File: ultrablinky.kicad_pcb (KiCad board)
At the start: 2 copper layers, 125 x 135 mm, 126 parts, among them J1 DNP, J2 SJ1-3523N, J3 SJ1-3523N, J4 Barrel_Jack_5.5x2.5, J5 DNP, J6 DNP, J7 Conn_01x05, J8 SJ1-3523N, Q1 DMP6180SK3Q-13, Q2 DMP6180SK3Q-13, Q4 MMBT3906, Q5 MMBT3904, Q6 MMBT3904, Q7 IRFZ44ZPBF, Q8 MMBT3904, SW1 SW_SPDT, SW2 PEC11R-4215F-S0024, SW3 SW_Push, U1 SGTL5000, U10 74VHC1G09, U2 TPS73618DBV, U3 Teensy4.0, U4 4N25, U5 LM2574HVM-5, U6 MC34071ADR2G, U7 DNP, U8 MCP4706A1T-E/CH, U9 VXO7803-500

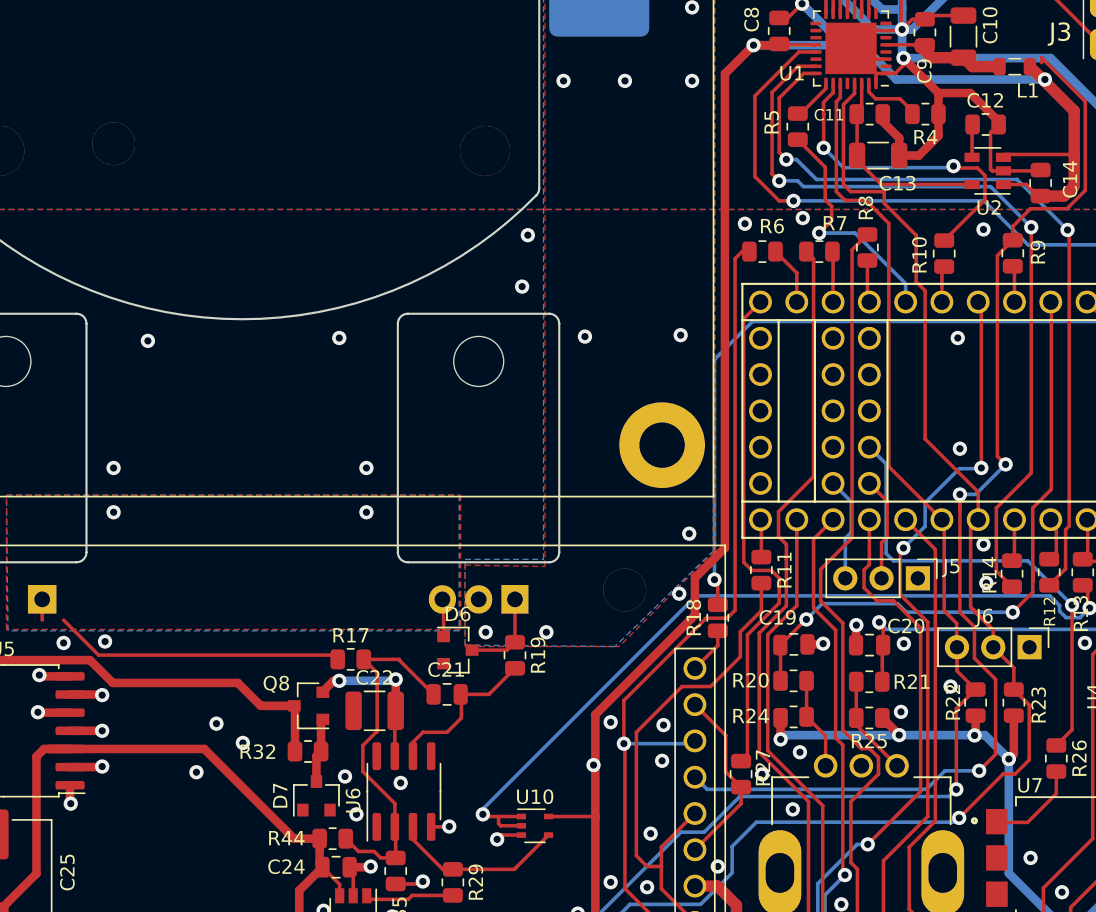
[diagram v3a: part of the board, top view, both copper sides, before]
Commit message: Added two additional bypass caps
The voltage regulator for the op amp and the 74VHC1G09 did not have
bypass caps previously
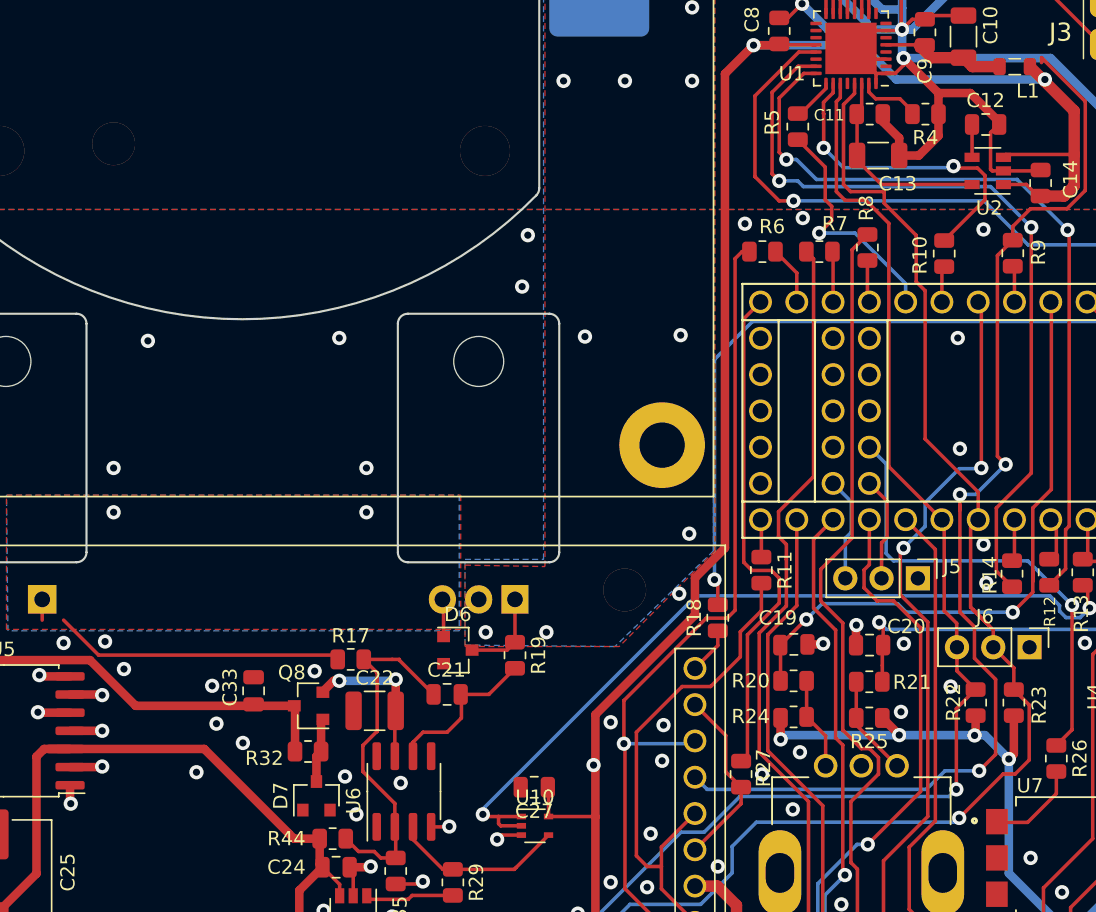
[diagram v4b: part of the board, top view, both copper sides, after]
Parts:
- added C27: 10nF, Capacitor_SMD:C_0805_2012Metric, F.Cu at (128.6, 121.5)
- added C33: 10nF, Capacitor_SMD:C_0805_2012Metric, F.Cu at (108.9, 114.8)
- C12: footprint Resistor_SMD:R_0805_2012Metric -> Capacitor_SMD:C_0805_2012Metric
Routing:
- net +3V3: track 383.7 -> 385.8 mm
- net GND: vias 155 -> 158

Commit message: Eliminated 5v-3.3v regulator
The Teensy 4.0 has a 3.3V pin that can supply up to 250mA, so that is
now the source for 3.3V.
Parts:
- removed the C31 at (144.0, 154.7)
- removed C32: 22uF, Capacitor_SMD:C_1210_3225Metric
- removed the J5 at (155.4, 106.9)
- removed the U9 at (147.8, 155.7)
- U7: renamed from U10; footprint Package_TO_SOT_SMD:SOT-353_SC-70-5 -> Package_TO_SOT_SMD:SOT-353_SC-70-5_Handsoldering
- moved R13 2.18 mm to (162.4, 106.4)
- moved R12 1.89 mm to (160.1, 106.4)
- moved R16 1.43 mm to (170.1, 106.2)
- moved R14 1.33 mm to (165.6, 106.3)
- moved R15 1.23 mm to (167.8, 106.3)
- moved R6 0.90 mm to (145.4, 84.0), turned to 90 degrees
- moved C17 0.48 mm to (146.2, 111.6)
- renumbered C17 to C16, C19 to C17, C20 to C18, C33 to C19, C21 to C20, C22 to C21, C18 to C22, C27 to C23, C23 to C24, C24 to C25, C25 to C26, C26 to C27, C4 to C3, C16 to C31, C3 to C4, D6 to D2, D2 to D3, D3 to D4, D7 to D5, D4 to D6, D5 to D7, J6 to J5, J8 to J6, LOGO2 to LOGO1, LOGO1 to LOGO2, Q8 to Q3, R9 to R10, R14 to R12, R12 to R13, R13 to R14, R45 to R15, R15 to R16, R16 to R17, R17 to R20, R20 to R21, R21 to R22, R22 to R23, R23 to R24, R24 to R25, R25 to R26, R32 to R27, R26 to R28, R27 to R29, R44 to R30, R28 to R31, R35 to R32, R29 to R33, R30 to R34, R31 to R35, R33 to R36, R34 to R37, R36 to R38, R37 to R39, R38 to R40, R39 to R41, R40 to R42, R41 to R43, R42 to R44, R43 to R45, R10 to R9, U7 to U8, U8 to U9
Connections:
- U3 pad 16: Net-(U3-Pad16) -> +3V3
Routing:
- net GND: track 312.4 -> 282.8 mm, vias 158 -> 189
- net VDC: track 87.1 -> 62.2 mm
- net /T_CS: track 80.4 -> 64.6 mm
- net +5V: track 191.6 -> 178.0 mm
- net Net-(U3-Pad35): track 7.35 -> 0.00 mm
- net Net-(U3-Pad36): track 7.32 -> 0.00 mm
- net /COPI: track 61.4 -> 66.9 mm
- net /T_IRQ: track 47.6 -> 52.7 mm, vias 1 -> 2
- net /I2S_MCLK: track 66.6 -> 62.7 mm
- net /ENCB: track 43.8 -> 46.3 mm
- net /PWM: track 56.9 -> 54.4 mm
- net +3V3: track 385.8 -> 388.0 mm
- net /CIPO: track 35.6 -> 37.6 mm
- net /I2S_LRCLK: track 56.2 -> 57.9 mm
- net /I2S_BCLK: track 55.0 -> 56.5 mm
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
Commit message: General cleanup and generate Gerbers
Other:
- board text added: "github.com/geedotk/ultrablinky Licensed under CERN-OHL-P v2"

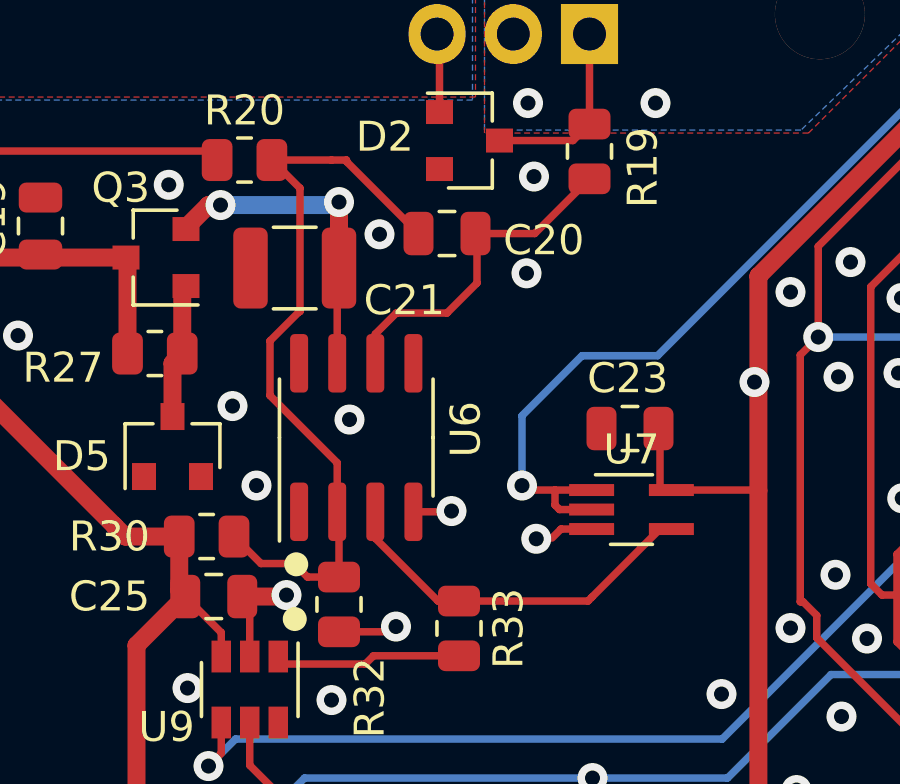
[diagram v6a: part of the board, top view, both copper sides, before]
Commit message: Changed 22uF cap to 10uF to reduce BOM cost
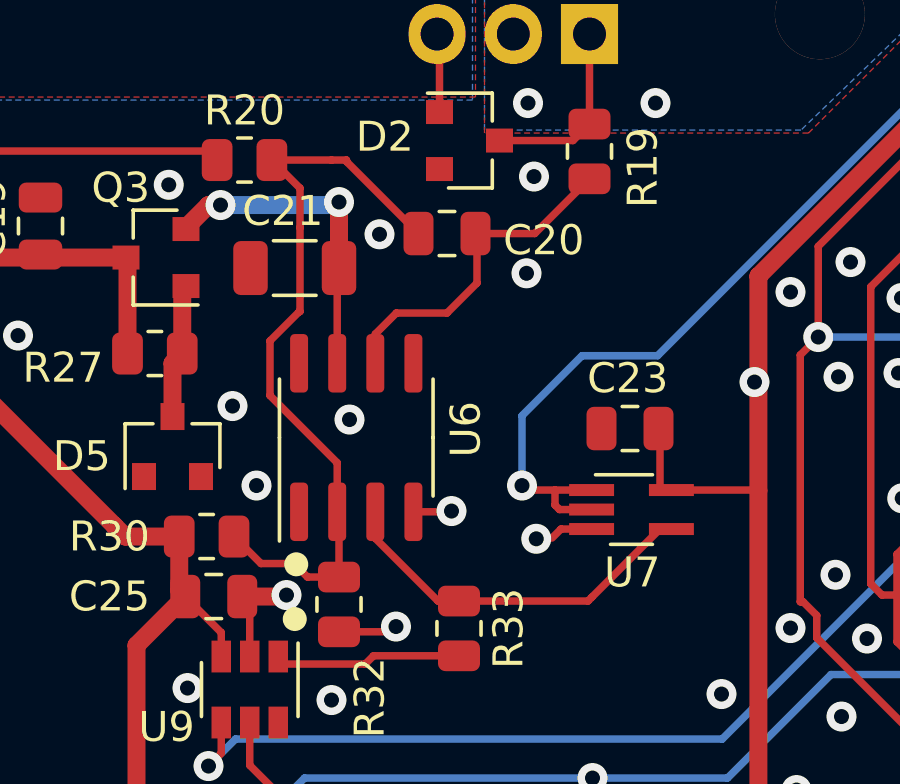
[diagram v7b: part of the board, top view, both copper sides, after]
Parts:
- C21: value 22uF -> 10uF; footprint Capacitor_SMD:C_1210_3225Metric -> Capacitor_SMD:C_1206_3216Metric

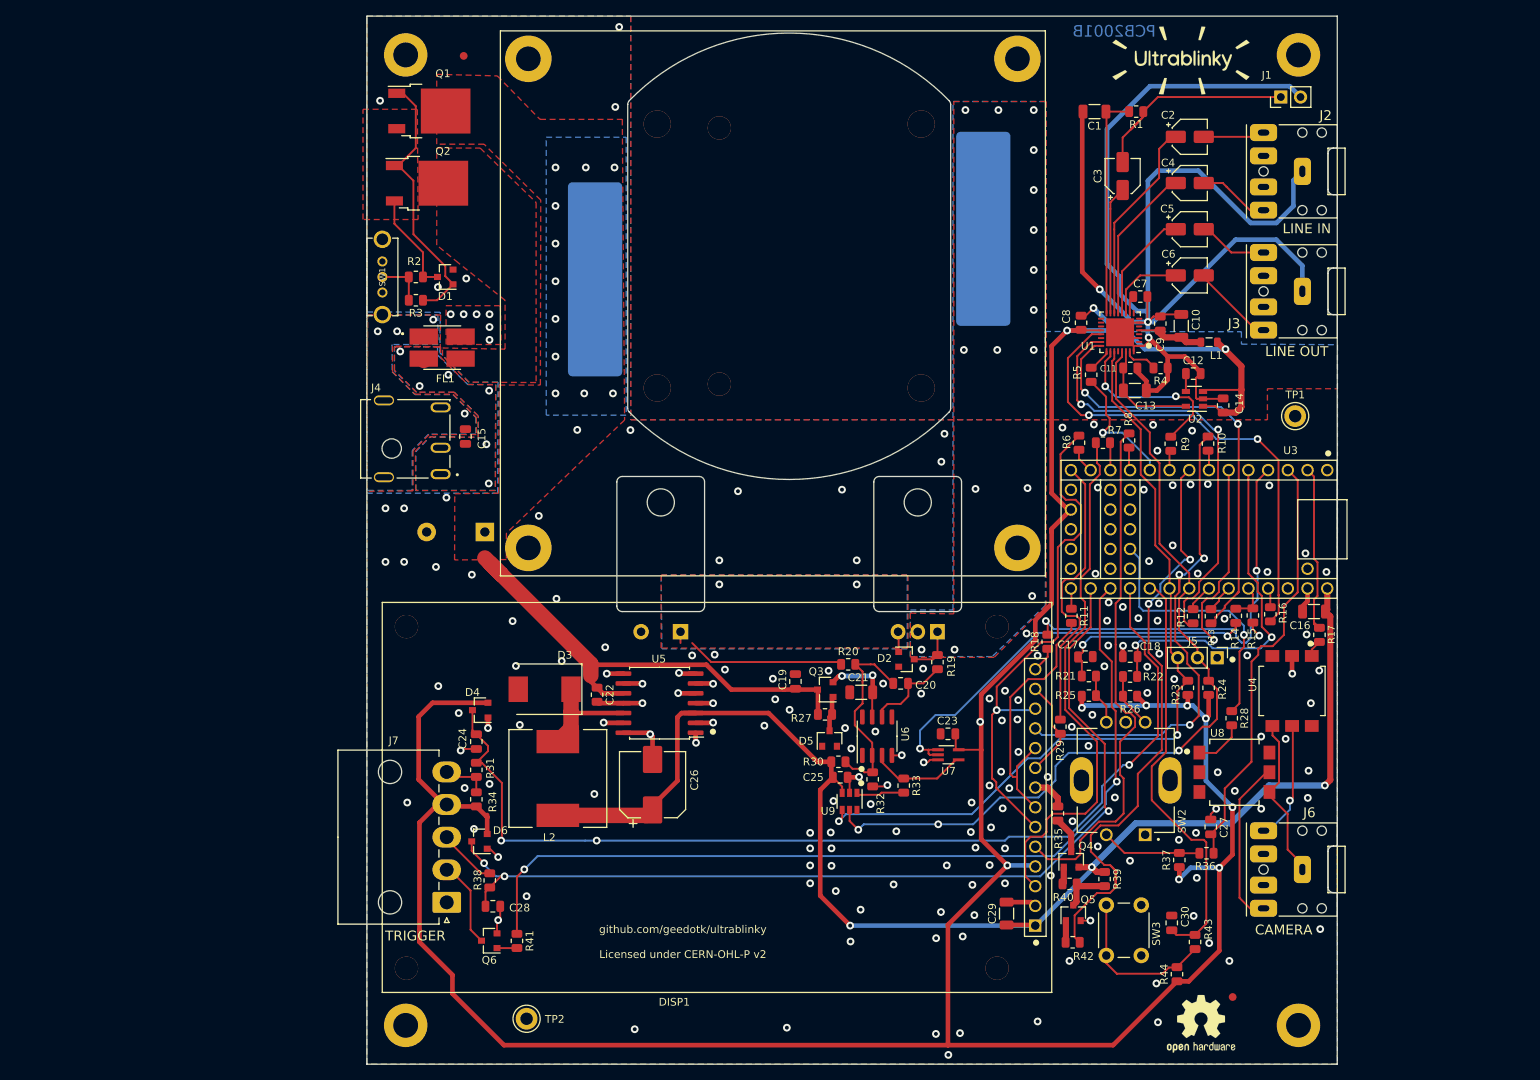
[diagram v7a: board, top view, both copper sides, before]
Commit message: Updated KiCad version to 6.0.2
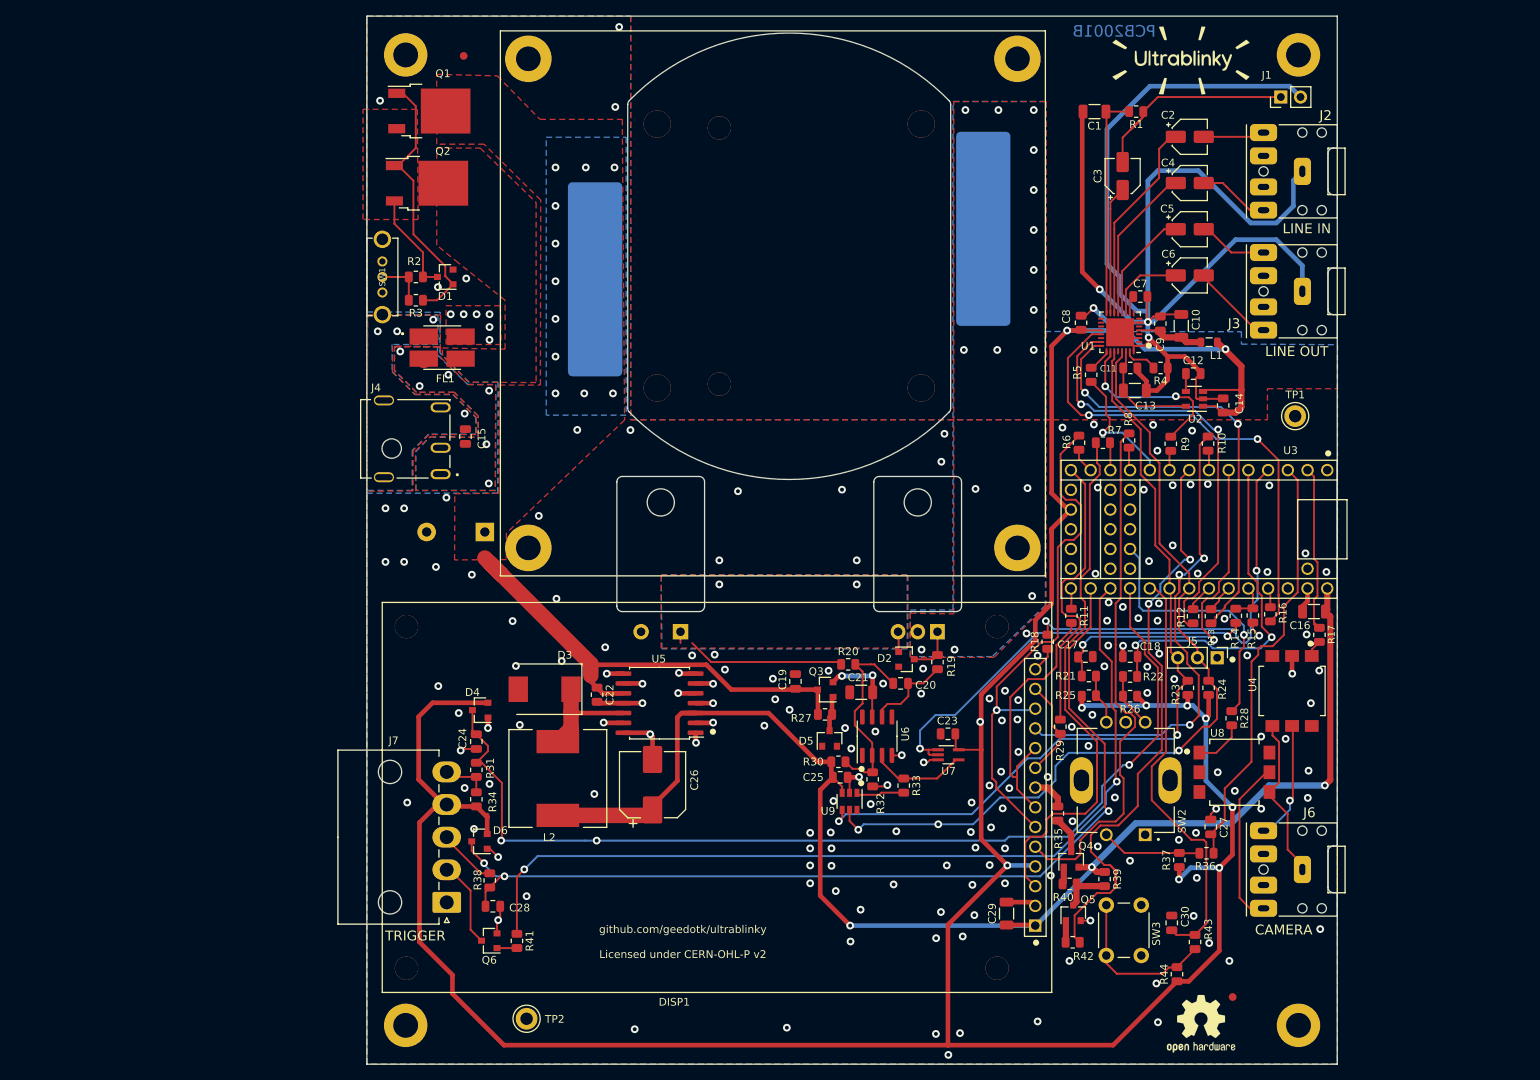
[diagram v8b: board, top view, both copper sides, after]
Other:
- net class Default removed
